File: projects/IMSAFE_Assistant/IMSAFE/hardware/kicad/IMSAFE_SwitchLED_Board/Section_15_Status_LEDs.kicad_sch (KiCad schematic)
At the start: 0 parts

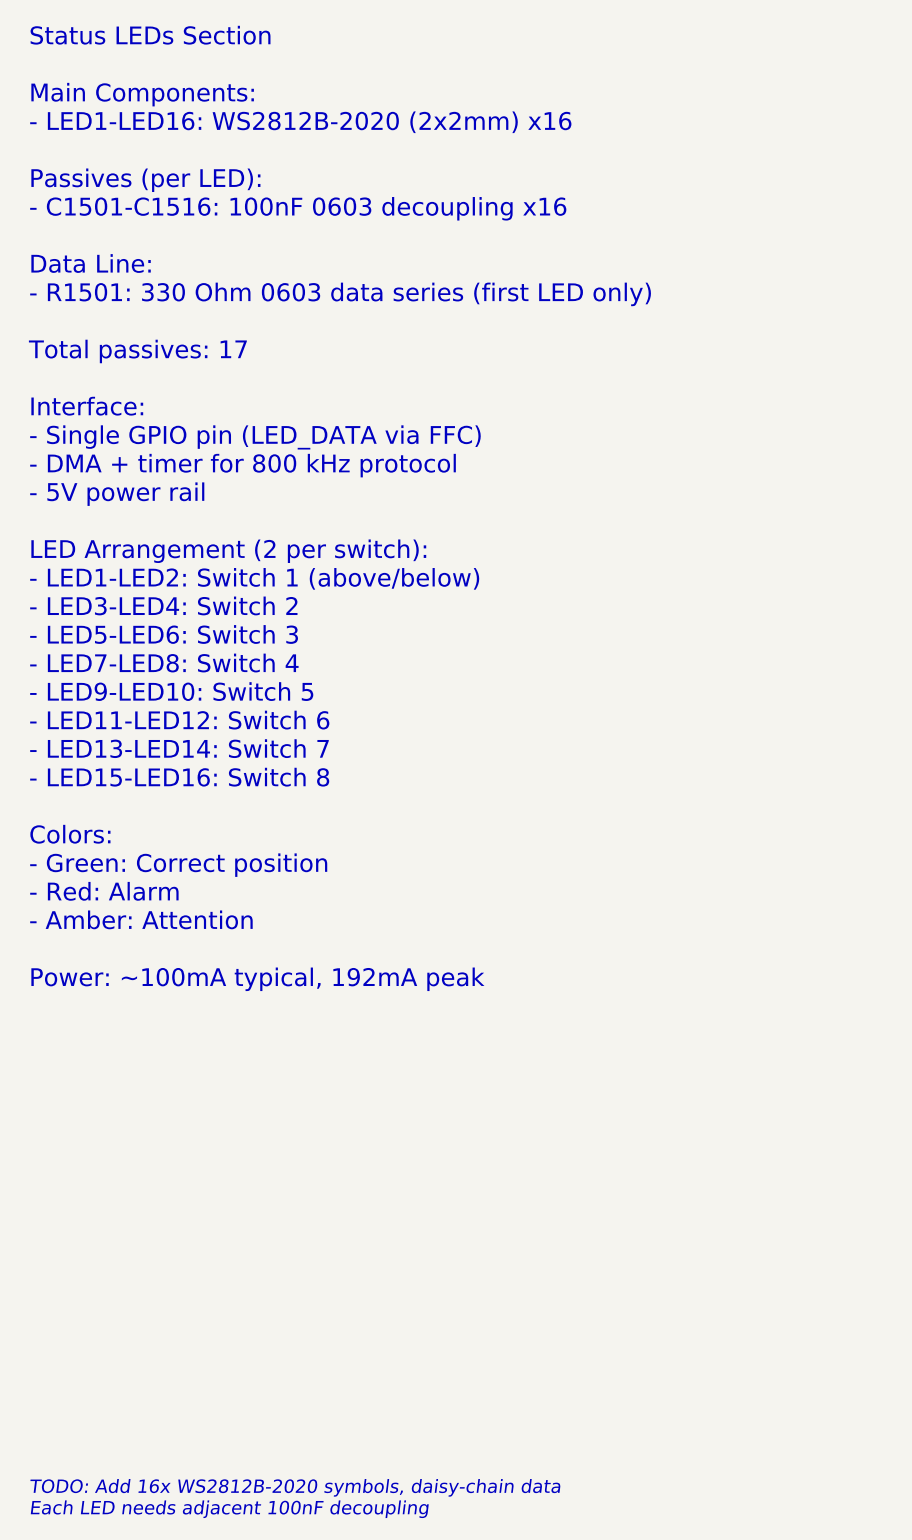
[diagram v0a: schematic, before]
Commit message: Update KiCad schematics and add analysis files
- Update all MainBoard schematic sections with component placement
- Add ERC reports and analysis scripts for schematic validation
- Update Radar Interface and SwitchLED Board projects
- Sync KiCad project files with latest session changes

Co-Authored-By: Claude Opus 4.5 <noreply@anthropic.com>
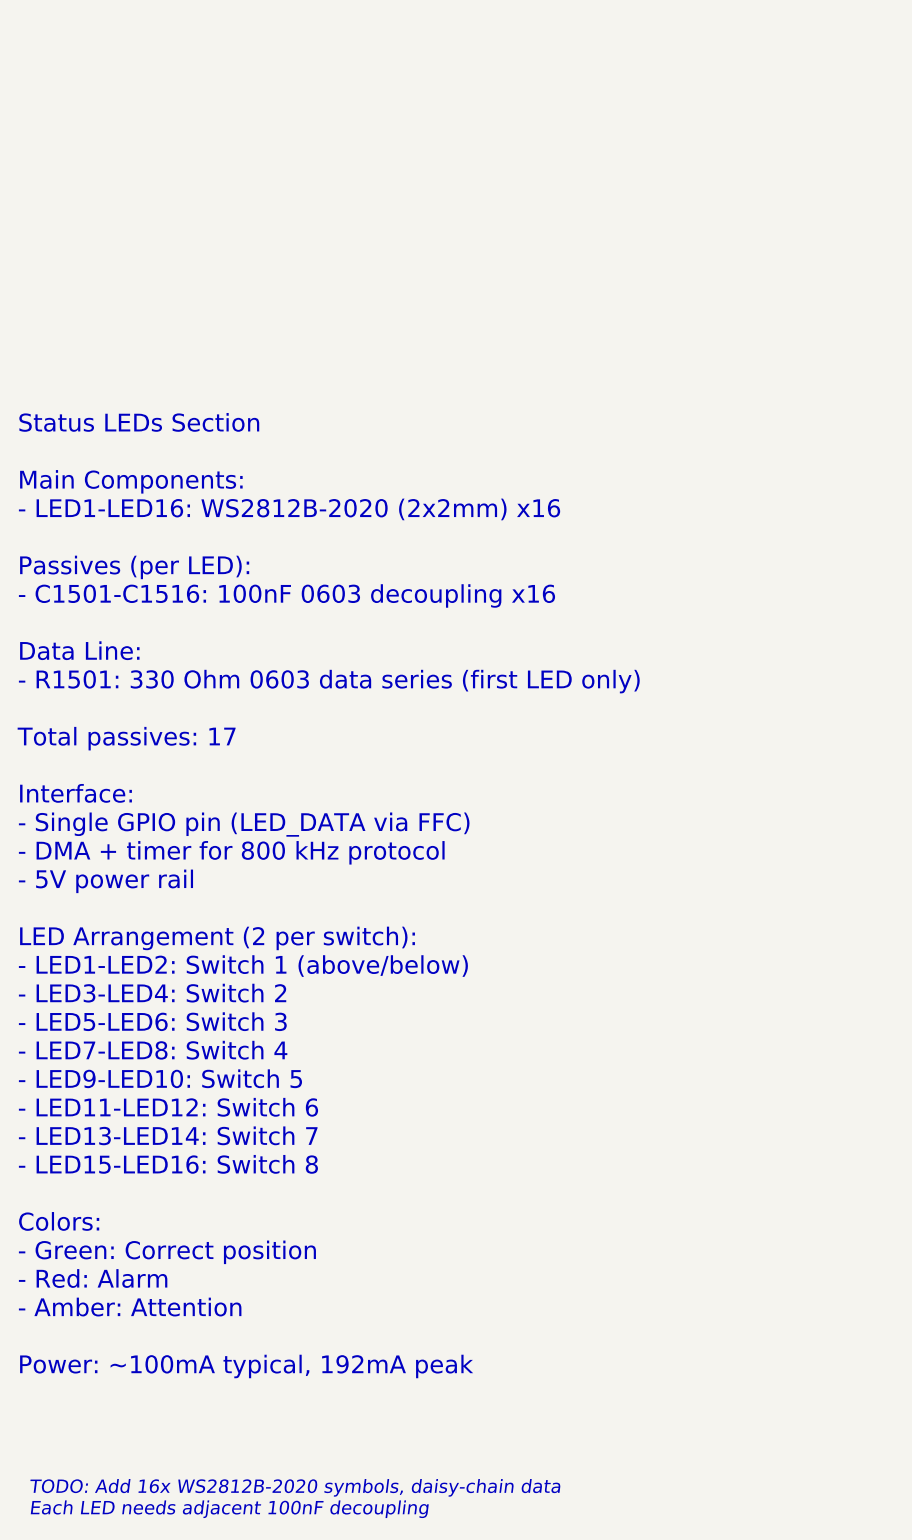
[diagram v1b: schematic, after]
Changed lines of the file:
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@@
 (kicad_sch
-	(version 20231120)
+	(version 20250114)
 	(generator "eeschema")
-	(generator_version "8.0")
-	(uuid "sec15-0001-0002-0003-000000000001")
+	(generator_version "9.0")
 	(paper "A4")
 	(title_block
@@
 		(comment 1 "WS2812B-2020 Addressable RGB LEDs")
 		(comment 2 "16 LEDs for switch status indication")
-	)
-	(text "Status LEDs Section\n\nMain Components:\n- LED1-LED16: WS2812B-2020 (2x2mm) x16\n\nPassives (per LED):\n- C1501-C1516: 100nF 0603 decoupling x16\n\nData Line:\n- R1501: 330 Ohm 0603 data series (first LED only)\n\nTotal passives: 17\n\nInterface:\n- Single GPIO pin (LED_DATA via FFC)\n- DMA + timer for 800 kHz protocol\n- 5V power rail\n\nLED Arrangement (2 per switch):\n- LED1-LED2: Switch 1 (above/below)\n- LED3-LED4: Switch 2\n- LED5-LED6: Switch 3\n- LED7-LED8: Switch 4\n- LED9-LED10: Switch 5\n- LED11-LED12: Switch 6\n- LED13-LED14: Switch 7\n- LED15-LED16: Switch 8\n\nColors:\n- Green: Correct position\n- Red: Alarm\n- Amber: Attention\n\nPower: ~100mA typical, 192mA peak"
-		(exclude_from_sim no)
-		(at 25.4 25.4 0)
-		(effects
-			(font
-				(size 2 2)
-			)
-			(justify left)
-		)
-		(uuid "sec15-text-001")
 	)
 	(text "TODO: Add 16x WS2812B-2020 symbols, daisy-chain data\nEach LED needs adjacent 100nF decoupling"
@@
 			(justify left)
 		)
-		(uuid "sec15-todo-001")
+	)
+	(text "Status LEDs Section\n\nMain Components:\n- LED1-LED16: WS2812B-2020 (2x2mm) x16\n\nPassives (per LED):\n- C1501-C1516: 100nF 0603 decoupling x16\n\nData Line:\n- R1501: 330 Ohm 0603 data series (first LED only)\n\nTotal passives: 17\n\nInterface:\n- Single GPIO pin (LED_DATA via FFC)\n- DMA + timer for 800 kHz protocol\n- 5V power rail\n\nLED Arrangement (2 per switch):\n- LED1-LED2: Switch 1 (above/below)\n- LED3-LED4: Switch 2\n- LED5-LED6: Switch 3\n- LED7-LED8: Switch 4\n- LED9-LED10: Switch 5\n- LED11-LED12: Switch 6\n- LED13-LED14: Switch 7\n- LED15-LED16: Switch 8\n\nColors:\n- Green: Correct position\n- Red: Alarm\n- Amber: Attention\n\nPower: ~100mA typical, 192mA peak"
+		(exclude_from_sim no)
+		(at 24.13 69.088 0)
+		(effects
+			(font
+				(size 2 2)
+			)
+			(justify left)
+		)
 	)
 )
